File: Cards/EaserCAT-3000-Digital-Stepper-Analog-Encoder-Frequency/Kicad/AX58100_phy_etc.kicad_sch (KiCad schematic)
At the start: 46 parts, among them U3 AMS1117-1.2

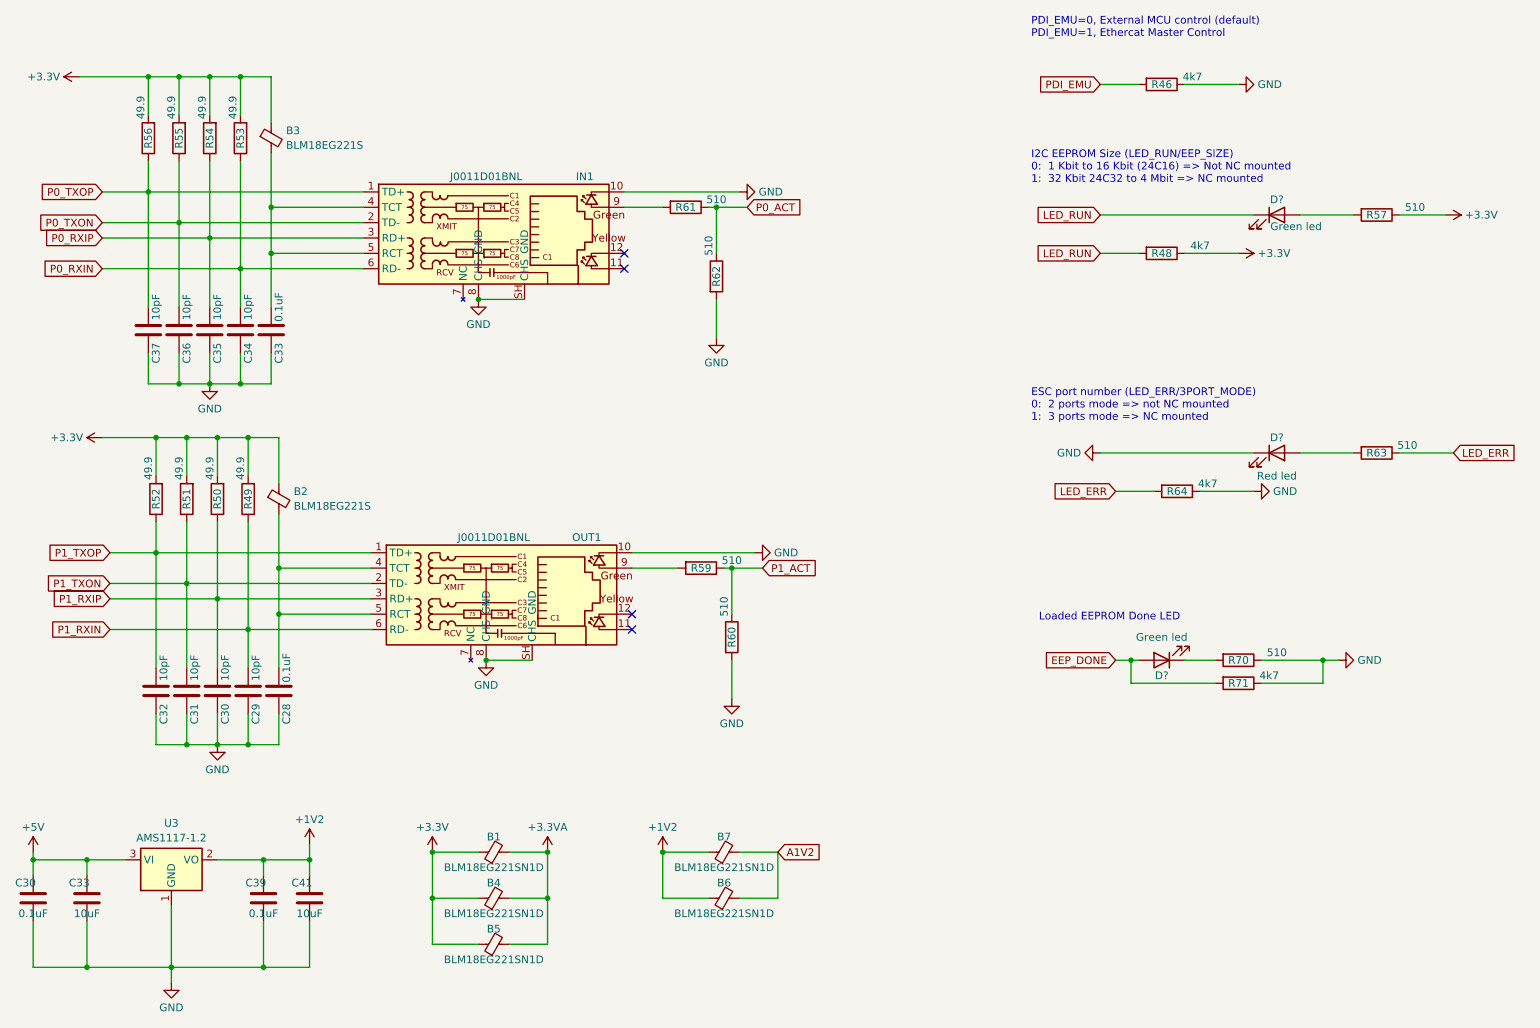
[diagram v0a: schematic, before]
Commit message: Moving all to Kicad8. Housekeeping symbols,libraries,3d-models
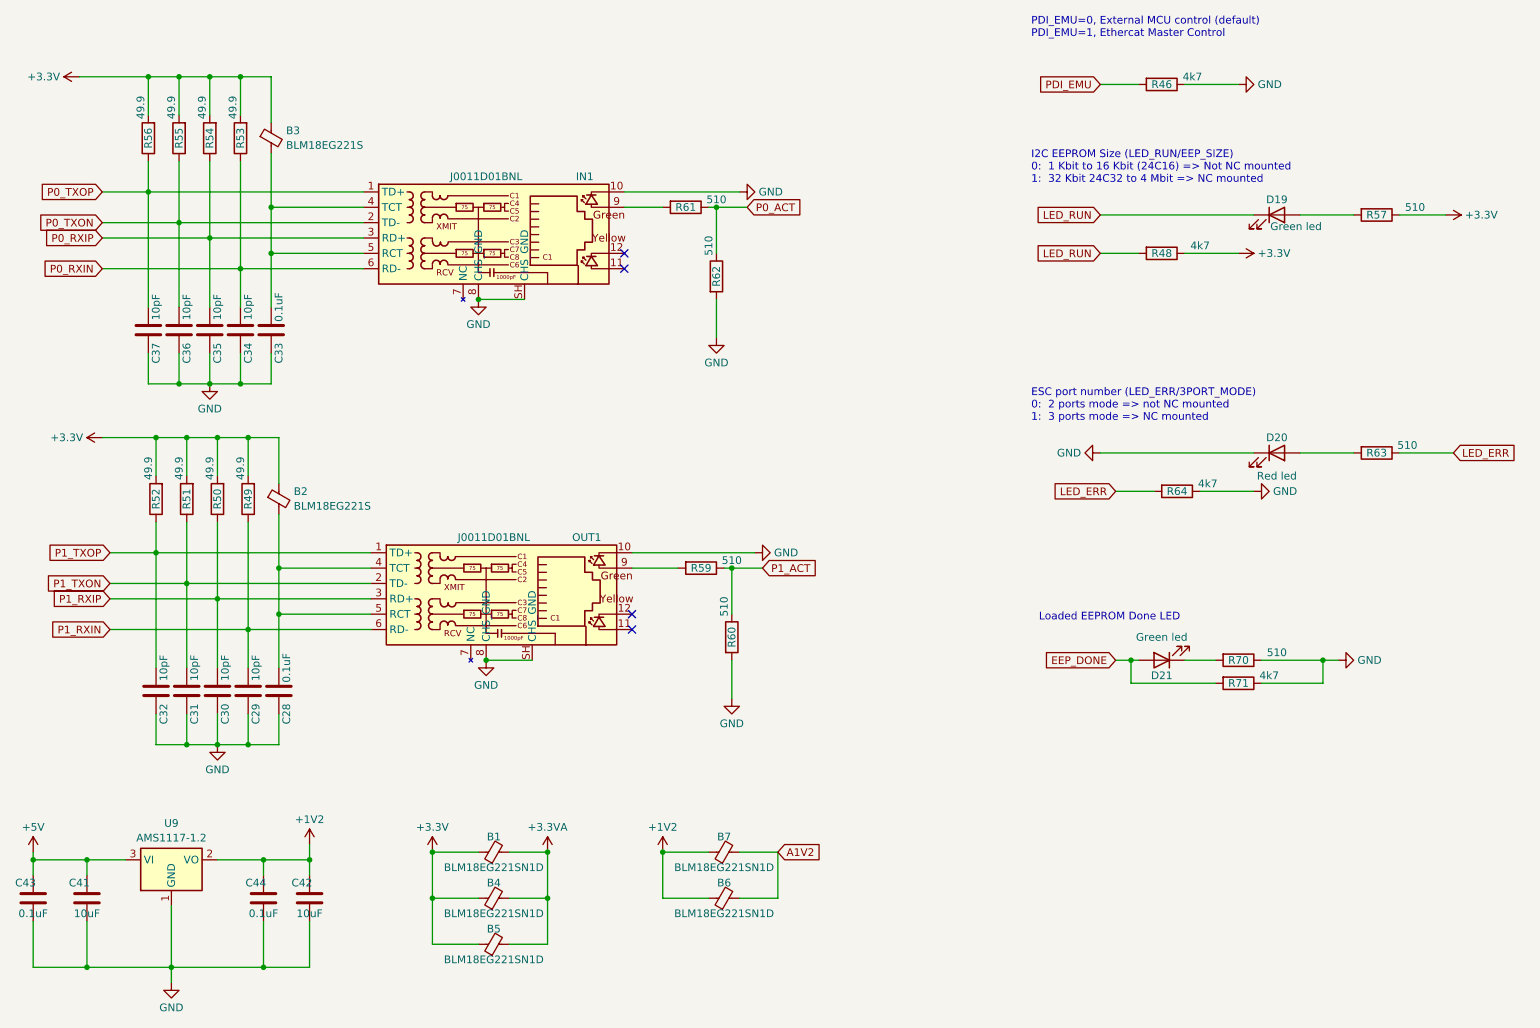
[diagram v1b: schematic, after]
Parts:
- gave numbers to parts that had none: 3
- renumbered C33 to C41, C41 to C42, C30 to C43, C39 to C44, U3 to U9
